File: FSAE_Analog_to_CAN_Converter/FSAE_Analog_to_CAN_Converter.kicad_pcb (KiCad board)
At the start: 4 copper layers, 49.8 x 41.5 mm, 32 parts, among them J1 Conn_01x10_Pin, U1 STM32F103RCTx, U2 MCP2561-E-MF, U3 AP63205WU, U4 LT1962-3.3

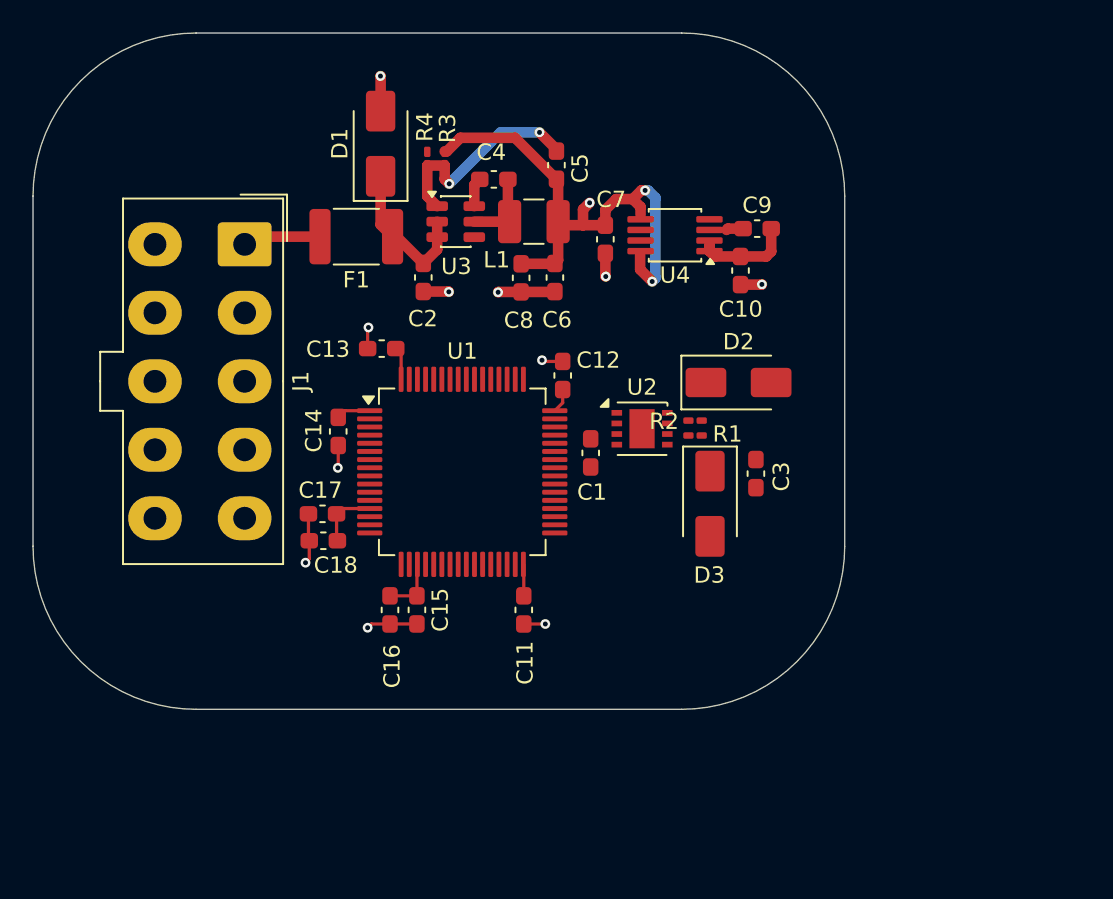
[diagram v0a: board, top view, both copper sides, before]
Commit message: added external clock, and SWD output header
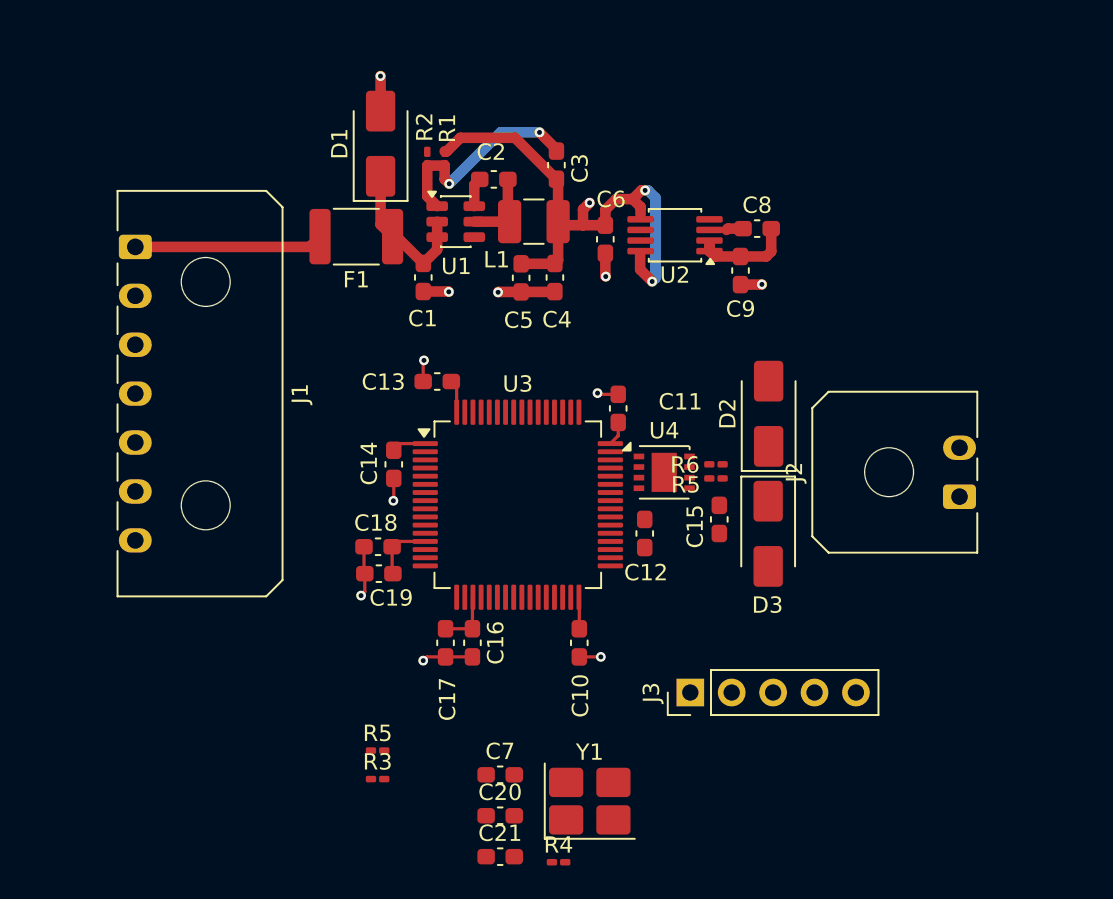
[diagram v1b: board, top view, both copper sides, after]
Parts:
- added C20: 10pF, Capacitor_SMD:C_0603_1608Metric_Pad1.08x0.95mm_HandSolder, F.Cu at (78.6, 73.1)
- added C21: 10pF, Capacitor_SMD:C_0603_1608Metric_Pad1.08x0.95mm_HandSolder, F.Cu at (78.6, 75.6)
- added C7: 0.1uF, Capacitor_SMD:C_0603_1608Metric_Pad1.08x0.95mm_HandSolder, F.Cu at (78.6, 70.6)
- added J2: Conn_01x02_Pin, Connector_Molex:Molex_Micro-Fit_3.0_43650-0200_1x02_P3.00mm_Horizontal, F.Cu at (106.8, 53.6)
- added J3: Conn_01x05, Connector_PinHeader_2.54mm:PinHeader_1x05_P2.54mm_Vertical, F.Cu at (90.3, 65.6)
- added R3: 10k, Resistor_SMD:R_0201_0603Metric_Pad0.64x0.40mm_HandSolder, F.Cu at (71.1, 70.9)
- added R4: 10k, Resistor_SMD:R_0201_0603Metric_Pad0.64x0.40mm_HandSolder, F.Cu at (82.2, 76.0)
- added R5: 10k, Resistor_SMD:R_0201_0603Metric_Pad0.64x0.40mm_HandSolder, F.Cu at (71.1, 69.1)
- added Y1: 8MHz, Crystal:Crystal_SMD_3225-4Pin_3.2x2.5mm_HandSoldering, F.Cu at (84.1, 72.2)
- J1: value Conn_01x10_Pin -> Conn_01x07_Pin; footprint Connector_Molex:Molex_Mini-Fit_Jr_5566-10A_2x05_P4.20mm_Vertical -> Connector_Molex:Molex_Micro-Fit_3.0_43650-0700_1x07_P3.00mm_Horizontal
- moved J1 6.71 mm to (56.2, 38.2)
- moved C12 5.95 mm to (87.5, 55.8)
- moved D3 4.02 mm to (95.0, 55.8)
- moved C10 3.96 mm to (83.5, 62.5)
- moved C11 3.96 mm to (85.9, 48.1)
- moved C13 3.96 mm to (74.8, 46.5)
- moved C14 3.96 mm to (72.1, 51.6)
- moved C16 3.96 mm to (76.9, 62.5)
- moved C17 3.96 mm to (75.3, 62.5)
- moved C18 3.96 mm to (71.1, 56.6)
- moved C19 3.96 mm to (71.2, 58.3)
- moved U3 3.96 mm to (79.7, 54.1)
- moved C15 3.60 mm to (92.1, 55.0)
- moved U4 3.00 mm to (88.7, 52.1)
- moved R6 2.97 mm to (91.8, 51.6)
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- renumbered C2 to C1, C11 to C10, C12 to C11, C1 to C12, C3 to C15, C15 to C16, C16 to C17, C17 to C18, C18 to C19, C4 to C2, C5 to C3, C6 to C4, C8 to C5, C7 to C6, C9 to C8, C10 to C9, R3 to R1, R4 to R2, R1 to R5, R2 to R6, U3 to U1, U4 to U2, U1 to U3, U2 to U4
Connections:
- D2 pad 1: /CAN_H -> Net-(D2-A1)
- D3 pad 1: /CAN_L -> Net-(D3-A1)
- R5 pad 1: /CAN_L -> Net-(D3-A1)
- R6 pad 2: /CAN_H -> Net-(D2-A1)
- U3 pad 46: unconnected-(U1-PA13-Pad46) -> /SWDIO
- U3 pad 49: unconnected-(U1-PA14-Pad49) -> /SWCLK
- U3 pad 5: unconnected-(U1-PD0-Pad5) -> /OSC_IN
- U3 pad 6: unconnected-(U1-PD1-Pad6) -> /OSC_OUT
- U3 pad 60: unconnected-(U1-BOOT0-Pad60) -> Net-(U3-BOOT0)
- U3 pad 7: unconnected-(U1-NRST-Pad7) -> /NRST
- U4 pad 6: /CAN_L -> Net-(D3-A1)
- U4 pad 7: /CAN_H -> Net-(D2-A1)
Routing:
- net Net-(J1-Pin_1): track 4.93 -> 11.6 mm
- added copper zone on In2.Cu, net +3.3V
- added copper zone on In1.Cu, net GND
- removed copper zone on In2.Cu, net GND
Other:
- board outline removed

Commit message: removed bottom portion of traces
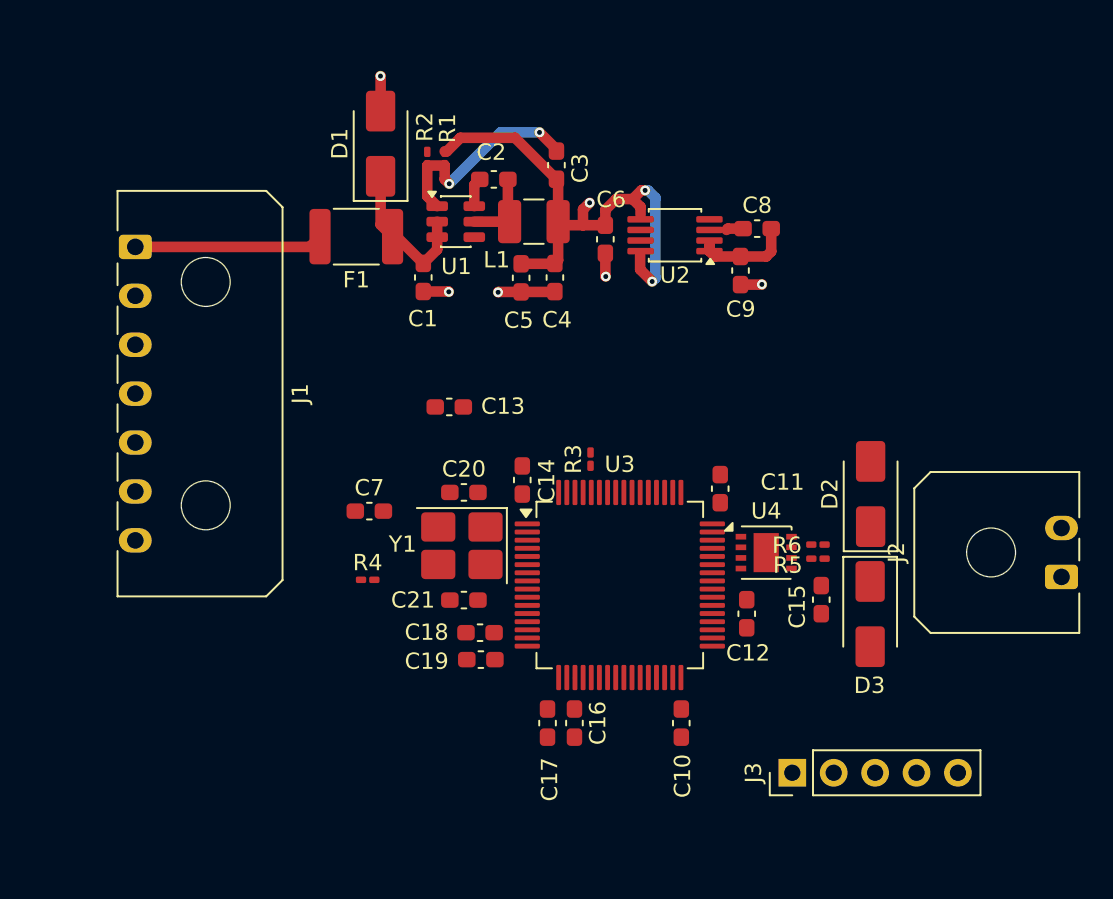
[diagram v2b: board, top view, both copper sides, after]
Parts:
- removed the R5 at (71.1, 69.1)
- moved R3 23.6 mm to (84.2, 51.3), turned to 90 degrees
- moved R4 20.9 mm to (70.5, 58.7)
- moved C20 20.0 mm to (76.4, 53.3)
- moved C7 18.1 mm to (70.6, 54.4)
- moved Y1 17.5 mm to (76.3, 56.6), turned to 180 degrees
- moved C21 15.9 mm to (76.4, 59.9), turned to 180 degrees
- moved C18 8.18 mm to (77.4, 61.9)
- moved C19 8.18 mm to (77.4, 63.6)
- moved C15 7.96 mm to (98.3, 59.9)
- moved J3 7.96 mm to (96.5, 70.5)
- moved R6 7.96 mm to (98.1, 56.5)
- moved U3 7.96 mm to (86.0, 59.0)
- moved C10 7.96 mm to (89.7, 67.4)
- moved C11 7.96 mm to (92.1, 53.1)
- moved C12 7.96 mm to (93.7, 60.7)
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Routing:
- net +3.3V: track 20.8 -> 6.42 mm
- net GND: track 21.5 -> 10.0 mm, vias 11 -> 5

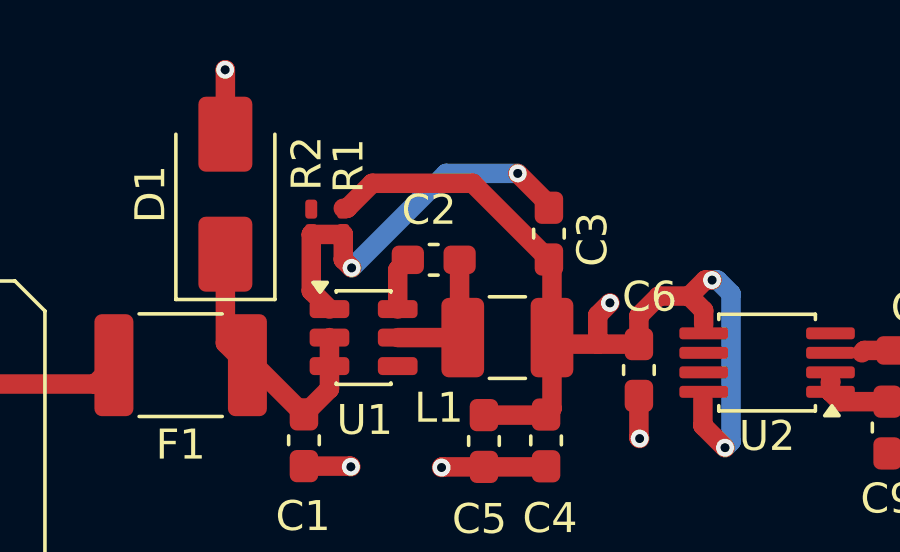
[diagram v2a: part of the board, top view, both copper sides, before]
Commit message: removed uneccesary stuff
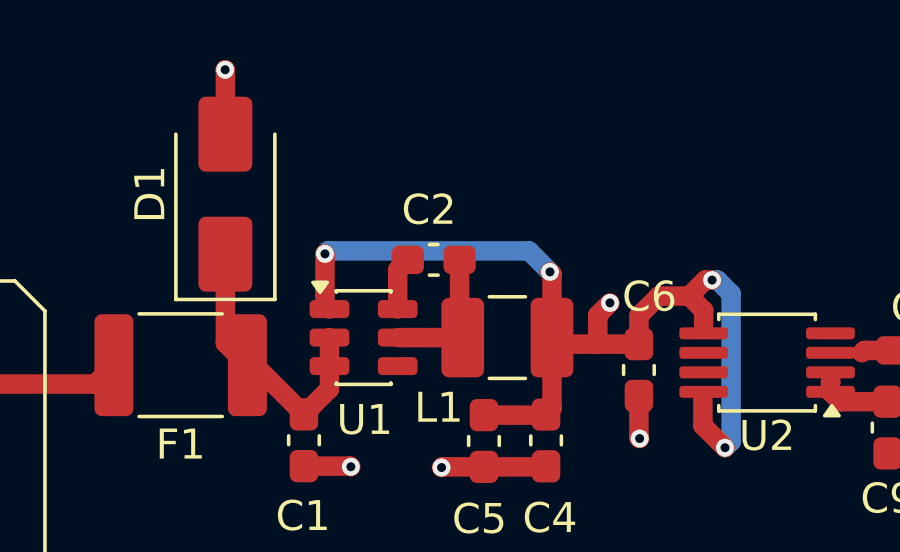
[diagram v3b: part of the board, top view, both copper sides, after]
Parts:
- removed C3: 100pF, Capacitor_SMD:C_0603_1608Metric_Pad1.08x0.95mm_HandSolder
- removed R1: 157k, Resistor_SMD:R_0201_0603Metric_Pad0.64x0.40mm_HandSolder
- removed R2: 30k, Resistor_SMD:R_0201_0603Metric_Pad0.64x0.40mm_HandSolder
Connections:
- U1 pad 1: Net-(U1-FB) -> +5V
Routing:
- net Net-(U1-FB): track 13.5 -> 0.00 mm, vias 2 -> 0
- net +5V: track 33.2 -> 34.2 mm, vias 3 -> 5

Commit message: almost done
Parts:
- removed the C12 at (93.7, 60.7)
- removed the C15 at (98.3, 59.9)
- removed D2, D3: SMAJ16A, Diode_SMD:D_SMA
- removed R4: 10k, Resistor_SMD:R_0201_0603Metric_Pad0.64x0.40mm_HandSolder
- removed R5, R6: 60, Resistor_SMD:R_0201_0603Metric_Pad0.64x0.40mm_HandSolder
- added C11: 100nF, Capacitor_SMD:C_0603_1608Metric_Pad1.08x0.95mm_HandSolder, F.Cu at (92.5, 56.2)
- added C13: 100nF, Capacitor_SMD:C_0603_1608Metric_Pad1.08x0.95mm_HandSolder, F.Cu at (88.3, 56.0)
- J2: footprint Connector_Molex:Molex_Micro-Fit_3.0_43650-0200_1x02_P3.00mm_Horizontal -> Connector_Molex:Molex_Micro-Fit_3.0_43045-0212_2x01_P3.00mm_Vertical
- U4: value MCP2561-E-MF -> MCP2562-E-MF
- Y1: footprint Crystal:Crystal_SMD_3225-4Pin_3.2x2.5mm_HandSoldering -> Crystal:Crystal_SMD_2012-2Pin_2.0x1.2mm_HandSoldering
- moved J2 16.9 mm to (97.9, 51.0), turned to 0 degrees
- moved C20 9.51 mm to (68.9, 54.0), turned to 0 degrees
- moved C16 7.77 mm to (75.1, 63.1)
- moved C15 7.77 mm to (76.8, 63.1)
- moved J3 7.70 mm to (99.5, 63.4), turned to -90 degrees
- moved C19 7.55 mm to (68.9, 52.1)
- moved C14 7.40 mm to (76.5, 46.0)
- moved R1 7.26 mm to (78.6, 46.5)
- moved C10 7.13 mm to (86.6, 48.6)
- moved U3 7.13 mm to (80.4, 54.5)
- moved C9 7.13 mm to (84.2, 63.0)
- moved C17 6.68 mm to (71.2, 59.4), turned to -90 degrees
- moved C18 6.18 mm to (72.8, 59.5), turned to -90 degrees
- moved U4 6.13 mm to (90.8, 52.5)
- moved Y1 5.62 mm to (71.9, 53.0), turned to 90 degrees
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- renumbered C11 to C10, C13 to C12, C16 to C15, C17 to C16, C18 to C17, C19 to C18, C20 to C19, C21 to C20, C4 to C3, C5 to C4, C6 to C5, C7 to C6, C8 to C7, C9 to C8, C10 to C9, R3 to R1
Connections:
- net Net-(U3-PA11) renamed /CAN_RX
- net Net-(U3-PA12) renamed /CAN_TX
- C19 pad 2: /OSC_IN -> /OSC_P
- C20 pad 2: /OSC_OUT -> /OSC_N
- J2 pad 1: Net-(D3-A1) -> /CAN_OUT_P
- J2 pad 2: Net-(D2-A1) -> /CAN_OUT_N
- U3 pad 14: /AIN_1 -> unconnected-(U3-PA0-Pad14)
- U3 pad 15: /AIN_2 -> unconnected-(U3-PA1-Pad15)
- U3 pad 16: /AIN_3 -> unconnected-(U3-PA2-Pad16)
- U3 pad 17: /AIN_4 -> unconnected-(U3-PA3-Pad17)
- U3 pad 20: /AIN_5 -> unconnected-(U3-PA4-Pad20)
- U3 pad 23: unconnected-(U3-PA7-Pad23) -> /AIN_1
- U3 pad 24: unconnected-(U3-PC4-Pad24) -> /AIN_2
- U3 pad 25: unconnected-(U3-PC5-Pad25) -> /AIN_3
- U3 pad 26: unconnected-(U3-PB0-Pad26) -> /AIN_4
- U3 pad 27: unconnected-(U3-PB1-Pad27) -> /AIN_5
- U3 pad 41: Net-(U3-PA8) -> unconnected-(U3-PA8-Pad41)
- U3 pad 5: /OSC_IN -> /OSC_P
- U3 pad 6: /OSC_OUT -> /OSC_N
- U4 pad 5: Net-(U4-SPLIT) -> +3.3V
- U4 pad 6: Net-(D3-A1) -> /CAN_OUT_N
- U4 pad 7: Net-(D2-A1) -> /CAN_OUT_P
- U4 pad 8: Net-(U3-PA8) -> +3.3V
- Y1 pad 1: /OSC_IN -> /OSC_N
- Y1 pad 2: GND -> /OSC_P
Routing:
- net /AIN_1: track 0.00 -> 40.2 mm
- net /AIN_2: track 0.00 -> 39.6 mm
- net +3.3V: track 6.42 -> 45.8 mm, vias 0 -> 10
- net /AIN_3: track 0.00 -> 37.7 mm
- net /AIN_4: track 0.00 -> 36.6 mm
- net /AIN_5: track 0.00 -> 35.9 mm
- net GND: track 10.0 -> 45.3 mm, vias 5 -> 24
- net /SWCLK: track 0.00 -> 26.7 mm, vias 0 -> 1
- net /NRST: track 0.00 -> 24.8 mm, vias 0 -> 1
- net /SWDIO: track 0.00 -> 19.4 mm, vias 0 -> 1
- net +5V: track 34.2 -> 42.1 mm, vias 5 -> 8
- net /CAN_OUT_N: track 0.00 -> 6.21 mm
- net /CAN_OUT_P: track 0.00 -> 6.21 mm
- net /OSC_N: track 0.00 -> 5.24 mm
- net /OSC_P: track 0.00 -> 5.24 mm
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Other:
- board outline added: 51.5 x 42.9 mm

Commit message: production files and no DRC errors
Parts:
- removed U4: MCP2562-E-MF, Package_DFN_QFN:DFN-8-1EP_3x3mm_P0.65mm_EP1.55x2.4mm
- added U5: MCP2562-E-SN, Package_SO:SOIC-8_3.9x4.9mm_P1.27mm, F.Cu at (92.5, 52.5)
- R1: footprint Resistor_SMD:R_0201_0603Metric_Pad0.64x0.40mm_HandSolder -> Resistor_SMD:R_0805_2012Metric_Pad1.20x1.40mm_HandSolder
- moved C11 3.19 mm to (95.4, 57.6)
- moved J2 3.16 mm to (101.1, 51.0)
- moved C13 1.77 mm to (88.8, 57.7)
- moved R1 1.03 mm to (79.2, 45.7)
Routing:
- net +3.3V: track 45.8 -> 37.0 mm, vias 10 -> 8
- net GND: track 45.3 -> 48.1 mm, vias 24 -> 26
- net /SWDIO: track 19.4 -> 17.5 mm, vias 1 -> 0
- net +5V: track 42.1 -> 44.0 mm
- net /CAN_TX: track 3.43 -> 4.64 mm
- net /CAN_RX: track 3.43 -> 4.64 mm
- net Net-(U2-BYP): track 1.05 -> 2.10 mm
- net /CAN_OUT_P: track 6.21 -> 6.82 mm
- net /CAN_OUT_N: track 6.21 -> 6.82 mm
- added copper zone on In2.Cu, net +5V
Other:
- board size 51.5 x 42.9 mm -> 55 x 45 mm
- board text added: "3.3V"
- board text added: "CANH"
- board text added: "CANL"
- board text added: "GND"
- board text added: "NRST"
- board text added: "SWCLK"
- board text added: "SWDIO"
